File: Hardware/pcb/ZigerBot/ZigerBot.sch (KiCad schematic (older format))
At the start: 107 parts, among them J1 Motor A, J2 M Power, J3 Motor B, J4 4 Pin Male SR-04 Header, J5 USB_B_Micro, J6 3 Pin Male Servo Header, J7 3 Pin Male Servo Header, J8 3 Pin Male Servo Header, J9 3 Pin Male Servo Header, Q1 SMD-MOSFET-P-CH-20V-2A-FDN340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, SW1 SMD Button, SW2 SMD Button, SW3 SMD Button, SW4 SMD Button, U1 L7805CDT-TR, U2 DRV8833PW, U3 ATmega2560-16AU, U4 CP2102N-A01-GQFN24, Y1 16MHz Resonator

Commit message: LED-Matrix routed
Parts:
- removed D2, D6: SMD LED blue, ZigerBot:LED_0603, symbol Device:LED
- removed D3, D7: SMD LED yellow, ZigerBot:LED_0603, symbol Device:LED
- removed R11, R5: 1k, Resistors_SMD:R_0402, symbol SeeedOPL-Resistor:SMD-RES-1K-5%-1_8W_0805_
- added D2, D3: LED_Dual_2pin, LEDs:LED_D5.0mm, symbol Device:LED_Dual_2pin
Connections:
- net labels added: ExtPower, MotInA, MotInB, MotOutA, MotOutB
- wire segments 283 -> 268
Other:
- moved on the sheet: R10, R4
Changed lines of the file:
@@
 	5400 2100 5150 2100
 Wire Wire Line
-	5150 2100 5150 1900
-Wire Wire Line
-	5150 1550 5350 1550
-Wire Wire Line
-	5650 1550 5700 1550
-Wire Wire Line
-	6000 1550 6250 1550
-Wire Wire Line
-	6250 1550 6250 1900
-Wire Wire Line
-	6250 2100 5500 2100
-Wire Wire Line
-	5500 2100 5500 2600
-Wire Wire Line
-	5150 1900 5350 1900
-Connection ~ 5150 1900
-Wire Wire Line
-	5150 1900 5150 1550
-Wire Wire Line
-	5650 1900 5700 1900
-Wire Wire Line
-	6000 1900 6250 1900
-Connection ~ 6250 1900
-Wire Wire Line
-	6250 1900 6250 2100
-Wire Wire Line
 	5400 3150 5400 3200
-Wire Wire Line
-	5400 4050 5100 4050
-Wire Wire Line
-	5100 4050 5100 4350
-Wire Wire Line
-	5100 4350 5350 4350
-Wire Wire Line
-	5650 4350 5700 4350
-Wire Wire Line
-	6000 4350 6150 4350
-Wire Wire Line
-	6150 4350 6150 4100
-Wire Wire Line
-	5500 4100 5500 3400
-Wire Wire Line
-	5500 4100 6150 4100
-Wire Wire Line
-	5100 4350 5100 4700
-Wire Wire Line
-	5100 4700 5350 4700
-Connection ~ 5100 4350
-Wire Wire Line
-	5650 4700 5700 4700
-Wire Wire Line
-	6000 4700 6150 4700
-Wire Wire Line
-	6150 4700 6150 4350
-Connection ~ 6150 4350
-$Comp
-L Device:LED D2
-U 1 1 5BBD9A5E
-P 5850 1550
-F 0 "D2" H 5850 1650 45  0000 C CNN
-F 1 "SMD LED blue" H 5850 1400 45  0000 C CNN
-F 2 "ZigerBot:LED_0603" H 5850 1550 50  0001 C CNN
-F 3 "" H 5850 1550 50  0001 C CNN
-	1    5850 1550
-	-1   0    0    1
-$EndComp
 $Comp
 L SeeedOPL-Resistor:SMD-RES-1K-5%-1_8W_0805_ R4
 U 1 1 5BBE3CAB
-P 5500 1550
-F 0 "R4" H 5500 1724 45  0000 C CNN
-F 1 "1k" H 5500 1640 45  0000 C CNN
-F 2 "Resistors_SMD:R_0402" H 5500 1550 40  0001 C CNN
-F 3 "" H 5500 1550 40  0001 C CNN
-F 4 "RC0805JR-071KL" H 5530 1700 20  0001 C CNN "MPN"
-F 5 "301010311" H 5530 1700 20  0001 C CNN "SKU"
-	1    5500 1550
-	1    0    0    -1
-$EndComp
-$Comp
-L SeeedOPL-Resistor:SMD-RES-1K-5%-1_8W_0805_ R5
-U 1 1 5BBECE75
-P 5500 1900
-F 0 "R5" H 5500 2074 45  0000 C CNN
-F 1 "1k" H 5500 1990 45  0000 C CNN
-F 2 "Resistors_SMD:R_0402" H 5500 1900 40  0001 C CNN
-F 3 "" H 5500 1900 40  0001 C CNN
-F 4 "RC0805JR-071KL" H 5530 2050 20  0001 C CNN "MPN"
-F 5 "301010311" H 5530 2050 20  0001 C CNN "SKU"
-	1    5500 1900
+P 5300 1850
+F 0 "R4" H 5300 2024 45  0000 C CNN
+F 1 "1k" H 5300 1940 45  0000 C CNN
+F 2 "Resistors_SMD:R_0402" H 5300 1850 40  0001 C CNN
+F 3 "" H 5300 1850 40  0001 C CNN
+F 4 "RC0805JR-071KL" H 5330 2000 20  0001 C CNN "MPN"
+F 5 "301010311" H 5330 2000 20  0001 C CNN "SKU"
+	1    5300 1850
 	1    0    0    -1
 $EndComp
@@
 L SeeedOPL-Resistor:SMD-RES-1K-5%-1_8W_0805_ R10
 U 1 1 5BBF1EEE
-P 5500 4350
-F 0 "R10" H 5500 4524 45  0000 C CNN
-F 1 "1k" H 5500 4440 45  0000 C CNN
-F 2 "Resistors_SMD:R_0402" H 5500 4350 40  0001 C CNN
-F 3 "" H 5500 4350 40  0001 C CNN
-F 4 "RC0805JR-071KL" H 5530 4500 20  0001 C CNN "MPN"
-F 5 "301010311" H 5530 4500 20  0001 C CNN "SKU"
-	1    5500 4350
-	1    0    0    -1
-$EndComp
-$Comp
-L SeeedOPL-Resistor:SMD-RES-1K-5%-1_8W_0805_ R11
-U 1 1 5BBF1F96
-P 5500 4700
-F 0 "R11" H 5500 4874 45  0000 C CNN
-F 1 "1k" H 5500 4790 45  0000 C CNN
-F 2 "Resistors_SMD:R_0402" H 5500 4700 40  0001 C CNN
-F 3 "" H 5500 4700 40  0001 C CNN
-F 4 "RC0805JR-071KL" H 5530 4850 20  0001 C CNN "MPN"
-F 5 "301010311" H 5530 4850 20  0001 C CNN "SKU"
-	1    5500 4700
+P 5250 4350
+F 0 "R10" H 5250 4524 45  0000 C CNN
+F 1 "1k" H 5250 4440 45  0000 C CNN
+F 2 "Resistors_SMD:R_0402" H 5250 4350 40  0001 C CNN
+F 3 "" H 5250 4350 40  0001 C CNN
+F 4 "RC0805JR-071KL" H 5280 4500 20  0001 C CNN "MPN"
+F 5 "301010311" H 5280 4500 20  0001 C CNN "SKU"
+	1    5250 4350
 	1    0    0    -1
 $EndComp
@@
 Connection ~ 5400 3200
 Wire Wire Line
-	5400 3200 5400 4050
-Wire Wire Line
-	5500 2800 5700 2800
-Connection ~ 5500 2800
-Wire Wire Line
-	5500 2600 5700 2600
-Connection ~ 5500 2600
-Wire Wire Line
-	5500 2600 5500 2800
-Wire Wire Line
-	5500 2800 5500 2950
+	5400 3200 5400 3900
 $Comp
 L Device:R_Small R7
@@
 Text GLabel 5050 2750 2    50   Input ~ 0
 GND
-Wire Wire Line
-	5400 2100 5400 3050
 Wire Wire Line
 	4450 3050 5400 3050
@@
 Wire Wire Line
 	7950 1750 7950 1900
-$Comp
-L Device:LED D6
-U 1 1 5C8C851A
-P 5850 4350
-F 0 "D6" H 5850 4450 45  0000 C CNN
-F 1 "SMD LED blue" H 5850 4200 45  0000 C CNN
-F 2 "ZigerBot:LED_0603" H 5850 4350 50  0001 C CNN
-F 3 "" H 5850 4350 50  0001 C CNN
-	1    5850 4350
-	-1   0    0    1
-$EndComp
-$Comp
-L Device:LED D3
-U 1 1 5C8C89BF
-P 5850 1900
-F 0 "D3" H 5850 2000 45  0000 C CNN
-F 1 "SMD LED yellow" H 5850 1750 45  0000 C CNN
-F 2 "ZigerBot:LED_0603" H 5850 1900 50  0001 C CNN
-F 3 "" H 5850 1900 50  0001 C CNN
-	1    5850 1900
-	1    0    0    -1
-$EndComp
-$Comp
-L Device:LED D7
-U 1 1 5C8C8C58
-P 5850 4700
-F 0 "D7" H 5850 4800 45  0000 C CNN
-F 1 "SMD LED yellow" H 5850 4550 45  0000 C CNN
-F 2 "ZigerBot:LED_0603" H 5850 4700 50  0001 C CNN
-F 3 "" H 5850 4700 50  0001 C CNN
-	1    5850 4700
-	1    0    0    -1
-$EndComp
+Wire Wire Line
+	5400 2100 5400 2600
+Wire Wire Line
+	5700 2600 5400 2600
+Connection ~ 5400 2600
+Wire Wire Line
+	5400 2600 5400 3050
+Wire Wire Line
+	5700 2800 5500 2800
+Wire Wire Line
+	5500 2100 5500 2800
+Connection ~ 5500 2800
+Wire Wire Line
+	5500 2800 5500 2950
+Text Label 4550 2950 0    50   ~ 0
+MotOutA
+Text Label 4550 3050 0    50   ~ 0
+MotInA
+Text Label 4550 3150 0    50   ~ 0
+MotOutB
+Text Label 4550 3250 0    50   ~ 0
+MotInB
+Text Label 2250 2650 2    50   ~ 0
+ExtPower
+$Comp
+L Device:LED_Dual_2pin D2
+U 1 1 5BDF6676
+P 5750 1850
+F 0 "D2" H 5750 2246 50  0000 C CNN
+F 1 "LED_Dual_2pin" H 5750 2155 50  0000 C CNN
+F 2 "LEDs:LED_D5.0mm" H 5750 1850 50  0001 C CNN
+F 3 "~" H 5750 1850 50  0001 C CNN
+F 4 "LTL-293SJW" H 5750 1850 50  0001 C CNN "MPN"
+	1    5750 1850
+	1    0    0    -1
+$EndComp
+Wire Wire Line
+	6050 1850 6050 2100
+Wire Wire Line
+	6050 2100 5500 2100
+Wire Wire Line
+	5150 1850 5150 2100
+$Comp
+L Device:LED_Dual_2pin D3
+U 1 1 5BE22D7B
+P 5700 4350
+F 0 "D3" H 5700 4746 50  0000 C CNN
+F 1 "LED_Dual_2pin" H 5700 4655 50  0000 C CNN
+F 2 "LEDs:LED_D5.0mm" H 5700 4350 50  0001 C CNN
+F 3 "~" H 5700 4350 50  0001 C CNN
+F 4 "LTL-293SJW" H 5700 4350 50  0001 C CNN "MPN"
+	1    5700 4350
+	1    0    0    -1
+$EndComp
+Wire Wire Line
+	5100 3900 5400 3900
+Wire Wire Line
+	5100 3900 5100 4350
+Wire Wire Line
+	5500 3900 6150 3900
+Wire Wire Line
+	6150 3900 6150 4350
+Wire Wire Line
+	6150 4350 6000 4350
+Wire Wire Line
+	5500 3900 5500 3400
 $EndSCHEMATC

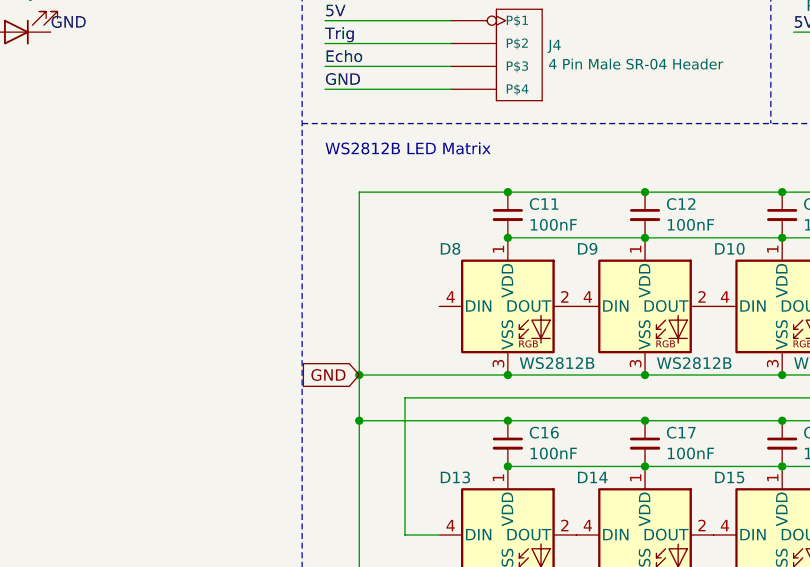
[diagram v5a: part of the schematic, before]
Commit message: changed pin mappings in README
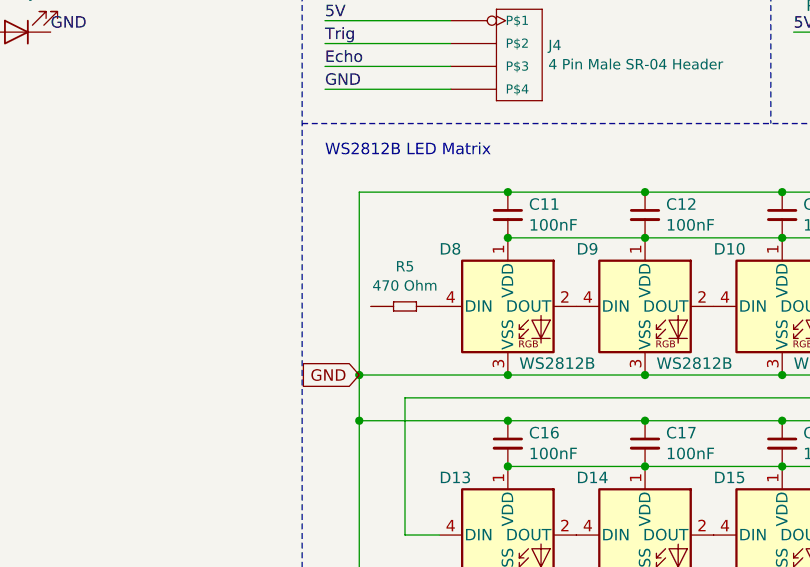
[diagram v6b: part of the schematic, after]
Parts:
- added R5: 470 Ohm, Resistors_SMD:R_0402, symbol SeeedOPL-Resistor:SMD-RES-100R-5%-1_8W_0805_
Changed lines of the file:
@@
 Wire Wire Line
 	5500 3900 5500 3400
+$Comp
+L SeeedOPL-Resistor:SMD-RES-100R-5%-1_8W_0805_ R5
+U 1 1 5BDB7850
+P 12300 4900
+F 0 "R5" H 12300 5074 45  0000 C CNN
+F 1 "470 Ohm" H 12300 4990 45  0000 C CNN
+F 2 "Resistors_SMD:R_0402" H 12300 4900 40  0001 C CNN
+F 3 "" H 12300 4900 40  0001 C CNN
+F 4 "RC0805JR-07100RL" H 12330 5050 20  0001 C CNN "MPN"
+F 5 "301010319" H 12330 5050 20  0001 C CNN "SKU"
+	1    12300 4900
+	1    0    0    -1
+$EndComp
 $EndSCHEMATC

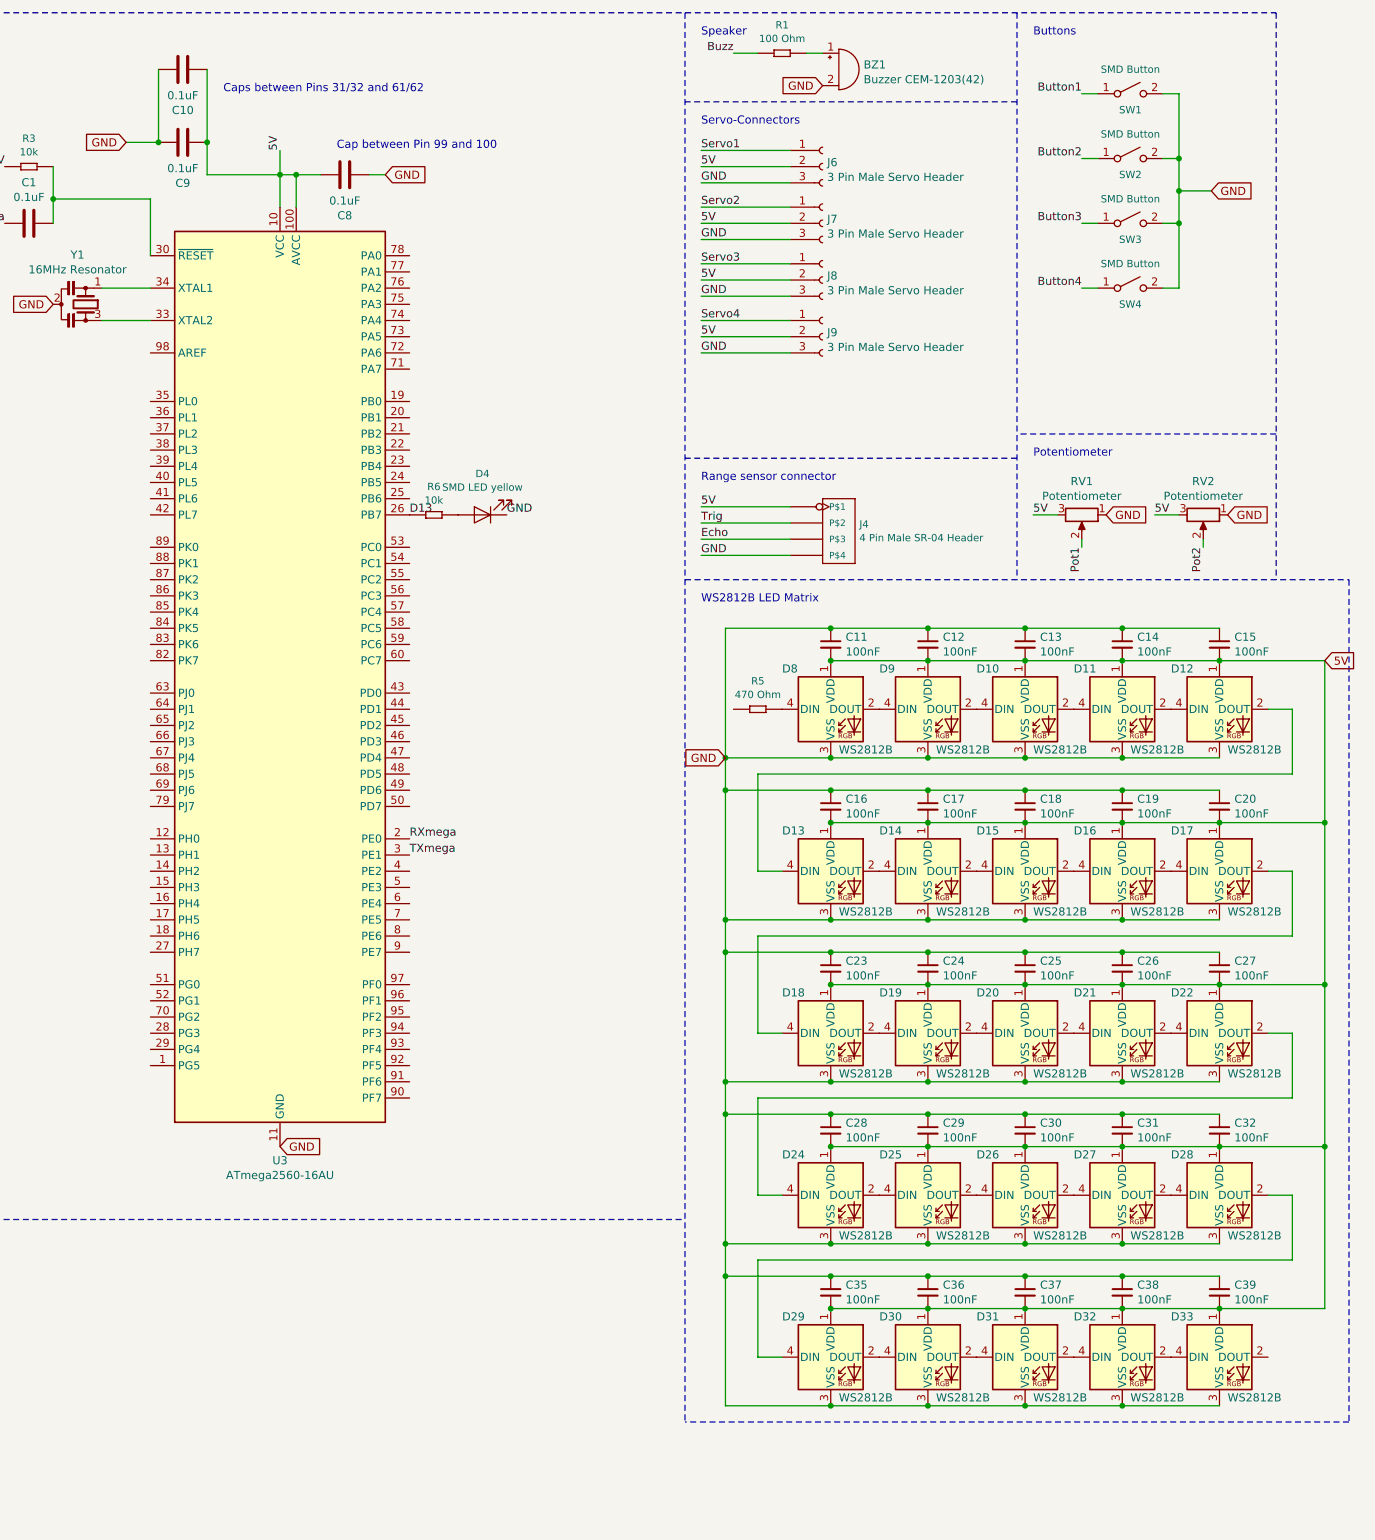
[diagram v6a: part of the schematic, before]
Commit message: Added ICSP Header, Connected all peripherals to Atmega2560, updated README.md
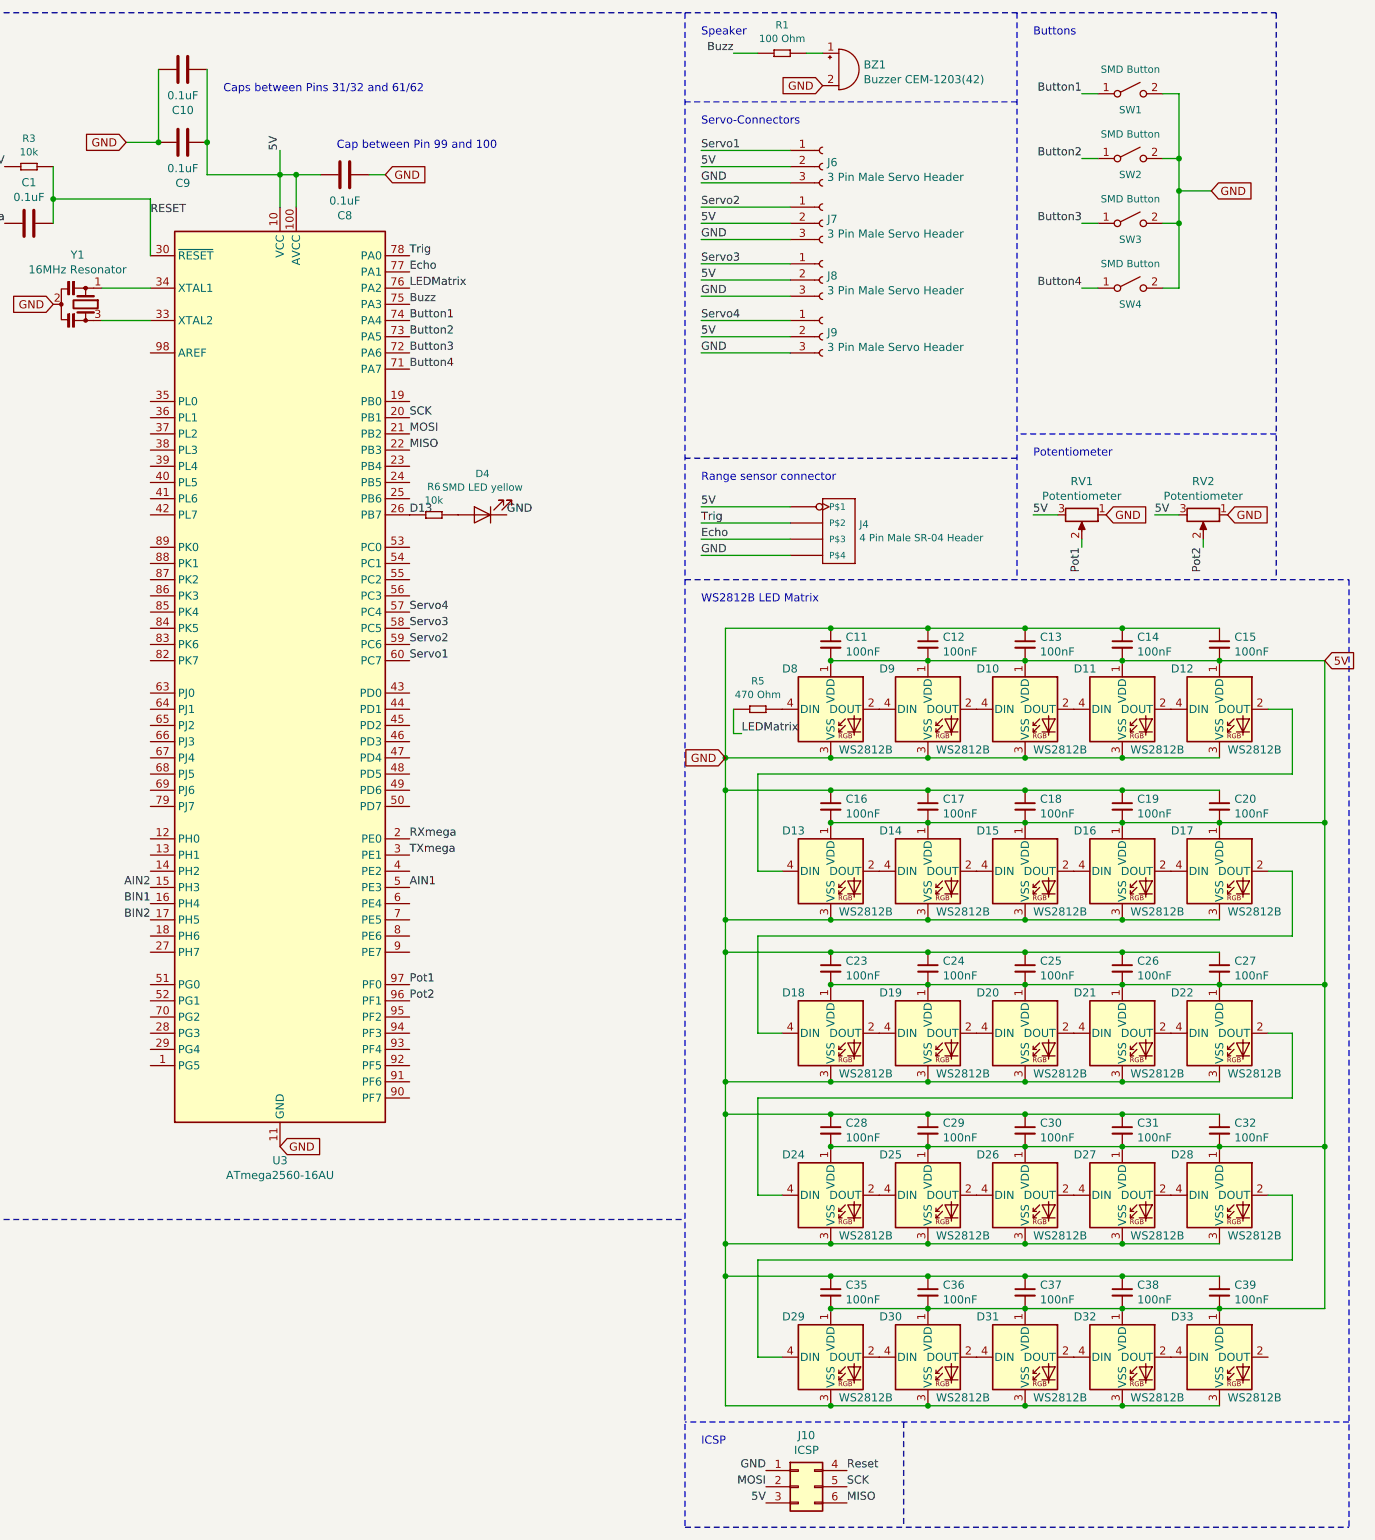
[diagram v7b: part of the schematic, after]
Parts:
- added J10: ICSP, ZigerBot:ICSP, symbol Connector_Generic:Conn_02x03_Top_Bottom
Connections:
- net labels added: LEDMatrix, MISO, MOSI, RESET, Reset, SCK
- wire segments 268 -> 270
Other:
- note added: "ICSP"
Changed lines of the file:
@@
 Text GLabel 4400 2350 3    50   Input ~ 0
 GND
-NoConn ~ 3250 2450
 Wire Wire Line
 	3250 2950 3150 2950
@@
 WS2812B LED Matrix
 Wire Notes Line
-	15950 4100 15950 9300
-Wire Notes Line
 	15950 9300 11850 9300
-Wire Notes Line
-	11850 600  11850 9300
 Wire Notes Line
 	11850 4100 15950 4100
@@
 	1    0    0    -1
 $EndComp
+Text Label 10150 4600 0    50   ~ 0
+Servo1
+Text Label 10150 4500 0    50   ~ 0
+Servo2
+Text Label 10150 4400 0    50   ~ 0
+Servo3
+Text Label 10150 4300 0    50   ~ 0
+Servo4
+Text Label 10150 2400 0    50   ~ 0
+Buzz
+Text Label 10150 2100 0    50   ~ 0
+Trig
+Text Label 10150 2200 0    50   ~ 0
+Echo
+Text Label 10150 2300 0    50   ~ 0
+LEDMatrix
+Wire Wire Line
+	12150 4900 12150 5050
+Wire Wire Line
+	12150 5050 12200 5050
+Text Label 12200 5050 0    50   ~ 0
+LEDMatrix
+Text Label 10150 2500 0    50   ~ 0
+Button1
+Text Label 10150 2600 0    50   ~ 0
+Button2
+Text Label 10150 2700 0    50   ~ 0
+Button3
+Text Label 10150 2800 0    50   ~ 0
+Button4
+NoConn ~ 3250 2450
+Text Label 10150 6000 0    50   ~ 0
+AIN1
+Text Label 8550 6000 2    50   ~ 0
+AIN2
+Text Label 8550 6100 2    50   ~ 0
+BIN1
+Text Label 8550 6200 2    50   ~ 0
+BIN2
+Text Label 10150 6600 0    50   ~ 0
+Pot1
+Text Label 10150 6700 0    50   ~ 0
+Pot2
+$Comp
+L Connector_Generic:Conn_02x03_Top_Bottom J10
+U 1 1 5BDFB83F
+P 12550 9700
+F 0 "J10" H 12600 10017 50  0000 C CNN
+F 1 "ICSP" H 12600 9926 50  0000 C CNN
+F 2 "ZigerBot:ICSP" H 12550 9700 50  0001 C CNN
+F 3 "~" H 12550 9700 50  0001 C CNN
+	1    12550 9700
+	1    0    0    -1
+$EndComp
+Text Label 12350 9600 2    50   ~ 0
+GND
+Text Label 10150 3200 0    50   ~ 0
+MOSI
+Text Label 10150 3300 0    50   ~ 0
+MISO
+Text Label 10150 3100 0    50   ~ 0
+SCK
+Text Label 8550 1850 0    50   ~ 0
+RESET
+Text Label 12350 9700 2    50   ~ 0
+MOSI
+Text Label 12350 9800 2    50   ~ 0
+5V
+Text Label 12850 9600 0    50   ~ 0
+Reset
+Text Label 12850 9700 0    50   ~ 0
+SCK
+Text Label 12850 9800 0    50   ~ 0
+MISO
+Wire Notes Line
+	11850 9950 15950 9950
+Wire Notes Line
+	15950 4100 15950 9950
+Wire Notes Line
+	11850 600  11850 9950
+Text Notes 11950 9450 0    50   ~ 0
+ICSP
+Wire Notes Line
+	13200 9300 13200 9950
 $EndSCHEMATC
